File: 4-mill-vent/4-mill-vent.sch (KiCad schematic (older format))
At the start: 73 parts, among them J1 Fan, J2 Buzzer, J3 Power, J4 ICSP, Q1 MMBT3904, Q2 MMBT3904, Q3 PZT3904, Q4 PZT3904, Q5 TSM480P06CP, Q6 MMBT3904, SW1 Power_off, SW2 Power_On, SW3 Fan_Down, SW4 Fan_Up, U1 LM321, U2 TSR_1-24120, U3 LM1117-5.0, U4 ATmega328P-AU, Y1 16.000MHZ

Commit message: Just pushing updates
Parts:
- added D14: 1N914, Diode_SMD:D_1206_3216Metric, symbol Diode:1N914
- added Q7: MMBT3904, Package_TO_SOT_SMD:SOT-23, symbol Transistor_BJT:MMBT3904
- added R24: 100k, Resistor_SMD:R_0603_1608Metric, symbol Device:R_Small_US
- D3: value SML4752HE3_A/I -> 833-3SMAJ5936B-TP
- R18: value 1k -> 10k
- U2: value TSR_1-24120 -> TPSM84212EAB
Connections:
- net +5V: now also R18.1
- net GND: now also Q7.2 (E)
- net Micro_power_Down: now also D14.2 (A); no longer R18.2
- net Monitor: now also SW2.1, D14.1 (K); no longer R18.1, U4.12 (PB0)
- net Motor: no longer U4.13 (PB1)
- net Up: now also R23.1
- net at R15.2, SW1.2: no longer SW2.1
- net at D13.2 (A), J3.1 (Pin_1): now also R24.2
- new net: Q7.1 (B), R24.1
- new net Ext_Power: Q7.3 (C), R18.2
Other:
- note added: "Batt Voltage Monitor\n30V in 4.5V out divided by 6.66\nfor 20V in the values are 33k and 8.2k for divide by 4\nThe input is clamped at 30v Max, over this the fuse will blow"
- note added: "Micro_Power_Down is active low output from the Micro.\nLatching this line low will power down the unit.\n\nMonitor is active low input to the Micro.\nWhen low this signals the Micro the Power_Off button is depressed\nUp is debounced in hardware.\nDo Not USE Int Pull Up.\n\nExt_Power is active low input to the Micro.\nWhen low this tell the Micro that an Ext Batt is in use.\nDo Not USE Int Pull Up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"
- note added: "Power Block:\n\nPin#1 Ext 30V Batt power \nPin#2 Return Batt Power\nPin#3 Int 30V Batt power"
- note removed: "1951-2612-ND"
- note removed: "Batt Voltage Monitor\n30V in 4.5V out divided by 6.66\nfor 20V in the values are 33k and 8.2k for divide by 4\nThe input is clamped at 33v Max, over this the fuse will blow"
- note removed: "Power Block:\n\nPin#1 INT 30V Batt power \nPin#2 Return Batt Power (Black)\nPin#3 EXT 30V Batt power"
- moved on the sheet: C10, C11, C12, C13, C14, C15, C16, C4, C7, C8, C9, D11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

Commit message: Just an update on things
update schematic to and pcb. figured out a way to user int, ext and chager over three pin connector with only to wires to PCB and no extra diode needed. getting closer to the anwers on PWM pins to use with what fuction.
very little let to do on PCB, but things have to get checked before getting it done.
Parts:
- removed D13: FM4004-W, Diode_SMD:D_SMB, symbol Diode:1N4003
- removed J3: Power, Connector_Molex:Molex_KK-254_AE-6410-03A_1x03_P2.54mm_Vertical, symbol Connector:Conn_01x03_Male
- removed Q7: MMBT3904, Package_TO_SOT_SMD:SOT-23, symbol Transistor_BJT:MMBT3904
- removed R18: 10k, Resistor_SMD:R_0603_1608Metric, symbol Device:R_Small_US
- removed R24: 100k, Resistor_SMD:R_0603_1608Metric, symbol Device:R_Small_US
- added BT1, BT2: Battery, symbol Device:Battery
- added J3: POWER_CONNECTOR, Connector_Molex:Molex_KK-254_AE-6410-02A_1x02_P2.54mm_Vertical, symbol Connector:Conn_01x02_Male
- added J5: Charger connector, symbol Connector:Conn_01x03_Female
- added J6: Ext connector, symbol Connector:Conn_01x03_Male
- added J7: Safety connector, symbol Connector:Conn_01x03_Female
- added J8: Power connector, symbol Connector:Conn_01x02_Female
- added J9: Ext batt connector, symbol Connector:Conn_01x03_Female
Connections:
- net GND: now also J3.1 (Pin_1)
- net Monitor: no longer C10.1, J4.3 (Pin_3), Q6.1 (B), R15.1, R16.1, SW2.1, U4.17 (PB5)
- net Up: no longer J4.4 (Pin_4), U4.15 (PB3)
- net at F1.1: now also J3.2 (Pin_2)
- net Timer_OC2B: now reaches U4.1 (PD3)
- net Timer_OC0A: now reaches U4.10 (PD6)
- net Timer_OC1A: now reaches U4.13 (PB1)
- net Timer_OC1B: now reaches U4.14 (PB2)
- net Timer_OC0B: now reaches U4.9 (PD5)
- net Down renamed Down+MOSO
- net Down+MOSO: now also J4.4 (Pin_4); no longer J4.1 (Pin_1)
- new net: J7.2 (Pin_2), J7.3 (Pin_3)
- new net: BT1.2 (-), J9.1 (Pin_1)
- new net: BT1.1 (+), J9.2 (Pin_2)
- new net: BT2.2 (-), J6.1 (Pin_1), J8.1 (Pin_1)
- new net: BT2.1 (+), J6.2 (Pin_2)
- new net: J6.3 (Pin_3), J8.2 (Pin_2)
- new net Monitor_SCLK: C10.1, J4.3 (Pin_3), Q6.1 (B), R15.1, R16.1, SW2.1, U4.17 (PB5)
- new net Timer_OC2A_MOSI: J4.1 (Pin_1), U4.15 (PB3)
- no-connect marks 1 -> 4
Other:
- note added: "Power Block:\n\nPin#1 Return Batt Power\nPin#2 Int 30V Batt power"
- note removed: "Power Block:\n\nPin#1 Ext 30V Batt power \nPin#2 Return Batt Power\nPin#3 Int 30V Batt power"
- moved on the sheet: D14, D3, F1, J1, J2, R4

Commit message: just keeping files up to date
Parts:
- removed D12: FM4004-W, Diode_SMD:D_SMB, symbol Diode:1N4003
- removed J2: Buzzer, Connector_Molex:Molex_KK-254_AE-6410-02A_1x02_P2.54mm_Vertical, symbol Connector:Conn_01x02_Male
- added D12: 1N914, Diode_SMD:D_1206_3216Metric, symbol Diode:1N914
- added D13: FM4004-W, Diode_SMD:D_SMB, symbol Diode:1N4003
- added J2: Buzzer, symbol Connector:Conn_01x03_Male
- C10: value 1uF -> T491C107M006AT; footprint Capacitor_SMD:C_1206_3216Metric -> Capacitor_Tantalum_SMD:CP_EIA-6032-15_Kemet-U
- C7: value LMK316AB7106MLHT -> 3.3uF
- C8: value C0603C104M4RACTU -> LMK316AB7106MLHT; footprint Capacitor_SMD:C_0603_1608Metric -> Capacitor_SMD:C_1206_3216Metric
- C9: value T491C107M006AT -> C0603C104M4RACTU; footprint Capacitor_Tantalum_SMD:CP_EIA-6032-15_Kemet-U -> Capacitor_SMD:C_0603_1608Metric
- J3: value POWER_CONNECTOR -> Power
- R12: value 100k -> 560k
- R15: value 1M -> 820k
- R16: value 10k -> 220k
- R17: value 47 -> 560k
- SW1: value Power_off -> Power_On
- SW2: value Power_On -> Power_off
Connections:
- net +12V: now also C9.1; no longer C7.1, R16.2
- net +5V: now also D13.1 (K)
- net Buzzer-: now also J2.1 (Pin_1)
- net GND: now also D14.2 (A), R17.2, SW2.1; no longer Q6.2 (E), R17.1, SW1.1
- net Micro_power_Down: now also D12.2 (A); no longer D14.2 (A)
- net Monitor: now also C7.1, Q6.1 (B), R15.1, R16.1, SW1.1; no longer D14.1 (K)
- net Monitor_SCLK: no longer C10.1, Q6.1 (B), R15.1, R16.1, SW2.1
- net Raw_Batt: now also R12.1, R13.2; no longer R12.2, R13.1
- net SW_Batt: now also J2.3 (Pin_3)
- net at Q5.1 (G), Q6.3 (C): now also R12.2; no longer R13.2
- net at SW2.2: now also R16.2, D12.1 (K); no longer R12.1
- net at SW1.2: now also R13.1; no longer R15.2
- net at U3.1 (GND): now also D14.1 (K); no longer R17.2
- net at D11.2 (A), U3.2 (VO): now also C10.1, R15.2, D13.2 (A); no longer C9.1
- net at J6.2 (Pin_2): now also J8.2 (Pin_2); no longer BT2.1 (+)
- net at J6.3 (Pin_3): now also BT2.1 (+); no longer J8.2 (Pin_2)
- net Error renamed LED4
- new net: Q6.2 (E), R17.1
- no-connect marks 4 -> 5
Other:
- note added: "6 Cell LiPo"
- note added: "Buzzer:\nPin#3 Buzzer -\nPin#2 N/C\nPin#1 Buzzer +"
- note added: "tested over 2 second delay off from full load to no load\n5v reg. set to 5.6v for diode drop."
- note removed: "Buzzer:\nPin#2 Buzzer -\nPin#1 Buzzer +"
- moved on the sheet: BT1, BT2, C1, C11, C12, C13, C14, C15, C16, C2, C3, C5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

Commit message: Board mainly done
Layout is done, have things to correct and adjustments to make, but for the most part it is done.
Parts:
- removed BT1, BT2: Battery, symbol Device:Battery
- removed J5: Charger connector, symbol Connector:Conn_01x03_Female
- removed J6: Ext connector, symbol Connector:Conn_01x03_Male
- removed J7: Safety connector, symbol Connector:Conn_01x03_Female
- removed J8: Power connector, symbol Connector:Conn_01x02_Female
- removed J9: Ext batt connector, symbol Connector:Conn_01x03_Female
- J2: footprint (none) -> Connector_Molex:Molex_KK-254_AE-6410-03A_1x03_P2.54mm_Vertical
- R5: value RN73H2BTTD4702B10 -> RN73H2BTTD4322F100
- R9: value RN73H2BTTD7061B10 -> RN73H2BTTD8061F50
- renumbered SW2 to SW1, SW1 to SW2
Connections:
- net Timer_OC0B is gone; now on net PWM: U4.9 (PD5)
- net Timer_OC1B is gone; now on net Up: U4.14 (PB2)
- net Timer_OC2B is gone; now on net RPM: U4.1 (PD3)
- net Alarm: now also U4.31 (PD1)
- net LED1: now also U4.23 (PC0)
- net LED2: now also U4.24 (PC1)
- net LED3: now also U4.25 (PC2)
- net LED4: now also U4.26 (PC3)
- net LED5: now also U4.27 (PC4)
- net LED6: now also U4.28 (PC5)
- net LED7: now also U4.30 (PD0)
- net Micro_power_Down: now also U4.11 (PD7)
- net Monitor: now also U4.2 (PD4)
- net Motor: now also U4.32 (PD2)
- net Down+MOSO renamed MOSO
- net MOSO: no longer R22.2
- net Monitor_SCLK renamed SCLK
- net REF: no longer names the net of U4.20 (AREF)
- net Timer_OC0A: no longer names the net of U4.10 (PD6)
- net Timer_OC1A renamed Down
- net Down: now also R22.2
- net Timer_OC2A_MOSI renamed MOSI
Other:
- note added: "Batt Voltage Monitor\nfor 24v the values are 43.2k (R5) and 8.06k (R9) for divide by 5\nfor 20V the values are 33k and 8.2k for divide by 4\nThe input is clamped at 30v Max, over this the fuse will blow"
- note removed: "6 Cell LiPo"
- note removed: "Batt Voltage Monitor\n30V in 4.5V out divided by 6.66\nfor 20V in the values are 33k and 8.2k for divide by 4\nThe input is clamped at 30v Max, over this the fuse will blow"
- moved on the sheet: J4, R21

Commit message: lastest updates to board
Board is done, just need to do more checking
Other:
- moved on the sheet: C11, C12, C13, C14, C15, C16, D10, D4, D5, D6, D7, D8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

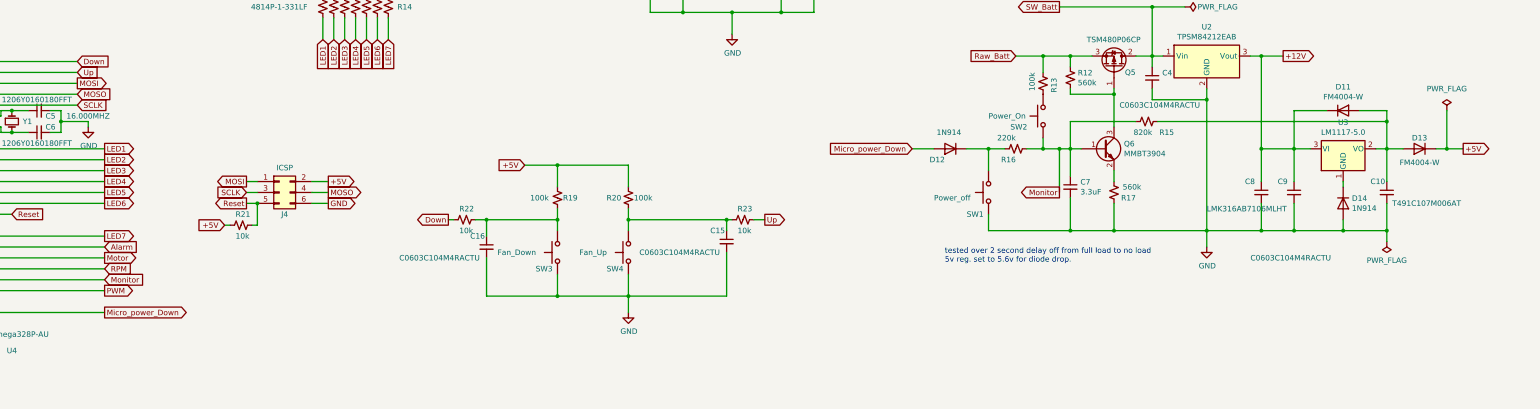
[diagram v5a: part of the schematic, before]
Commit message: Added more to design
Had to add a transitor for allow the micro to power down the unit.
The reason is Q6's base can be as high as 16v when the on button is pressed.
This micro does not have open collector outputs and that would blow the chip.
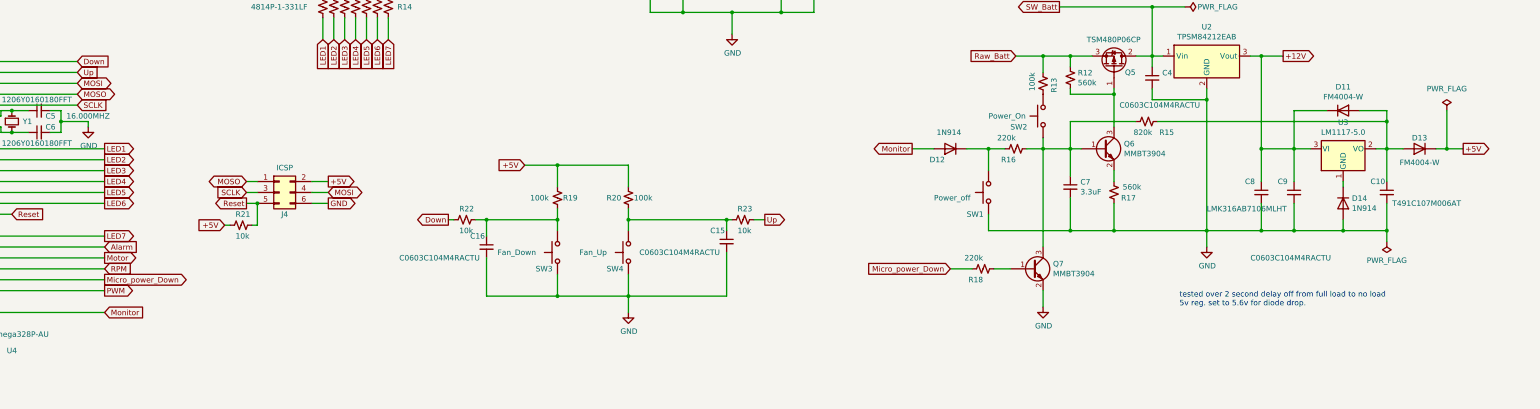
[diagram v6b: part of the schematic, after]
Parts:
- added Q7: MMBT3904, Package_TO_SOT_SMD:SOT-23, symbol Transistor_BJT:MMBT3904
- added R18: 220k, Resistor_SMD:R_0603_1608Metric, symbol Device:R_Small_US
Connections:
- net GND: now also Q7.2 (E)
- net MOSI: now also J4.4 (Pin_4); no longer J4.1 (Pin_1)
- net MOSO: now also J4.1 (Pin_1); no longer J4.4 (Pin_4)
- net Micro_power_Down: now also U4.2 (PD4), R18.2; no longer D12.2 (A), U4.11 (PD7)
- net Monitor: now also D12.2 (A), U4.11 (PD7); no longer C7.1, Q6.1 (B), R15.1, R16.1, SW2.1, U4.2 (PD4)
- new net: Q7.1 (B), R18.1
- new net: C7.1, Q6.1 (B), Q7.3 (C), R15.1, R16.1, SW2.1
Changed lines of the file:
@@
 Wire Wire Line
 	1150 3700 1150 3850
-Text GLabel 3300 4500 2    50   Input ~ 0
+Text GLabel 3300 4500 2    50   BiDi ~ 0
 MOSO
-Text GLabel 3300 4400 2    50   Output ~ 0
+Text GLabel 3300 4400 2    50   BiDi ~ 0
 MOSI
 $Comp
@@
 	9850 650  9850 900
 Connection ~ 10150 650
-Text GLabel 10950 5000 0    50   Input ~ 0
+Text GLabel 11300 6100 0    50   Input ~ 0
 Micro_power_Down
-Text GLabel 3550 6500 2    50   Output ~ 0
+Text GLabel 3550 6200 2    50   Output ~ 0
 Micro_power_Down
 Wire Wire Line
@@
 Text GLabel 3300 4600 2    50   Input ~ 0
 SCLK
-Text GLabel 12300 5400 0    50   Output ~ 0
+Text GLabel 10950 5000 0    50   Output ~ 0
 Monitor
 Text GLabel 6700 5650 0    50   Output ~ 0
@@
 Text GLabel 9600 5650 2    50   Output ~ 0
 Up
-Text GLabel 5600 5400 2    50   Output ~ 0
+Text GLabel 4850 5300 0    50   BiDi ~ 0
 MOSO
-Text GLabel 4850 5300 0    50   Output ~ 0
+Text GLabel 5600 5400 2    50   BiDi ~ 0
 MOSI
 Text GLabel 4850 5400 0    50   Input ~ 0
@@
 	0    -1   -1   0
 $EndComp
-Text Notes 11250 6050 0    50   ~ 0
+Text Notes 13400 6450 0    50   ~ 0
 tested over 2 second delay off from full load to no load\n5v reg. set to 5.6v for diode drop.
 Wire Wire Line
@@
 Connection ~ 12800 5750
 Wire Wire Line
-	12400 5000 12300 5000
-Wire Wire Line
 	12400 4150 12600 4150
 Wire Wire Line
@@
 Wire Wire Line
 	10950 5000 11150 5000
-Wire Wire Line
-	12300 5000 12300 5400
-Text GLabel 3550 6200 2    50   Input ~ 0
+Text GLabel 3550 6500 2    50   Input ~ 0
 Monitor
-Connection ~ 12300 5000
-Wire Wire Line
-	12300 5000 12150 5000
 Wire Wire Line
 	2500 5000 3550 5000
@@
 Wire Wire Line
 	13150 4450 13150 4550
+Wire Wire Line
+	12150 5000 12400 5000
+Wire Wire Line
+	11300 6100 11500 6100
+Wire Wire Line
+	12150 5000 12150 5900
+$Comp
+L Transistor_BJT:MMBT3904 Q7
+U 1 1 5F1B5AF9
+P 12050 6100
+F 0 "Q7" H 12241 6146 50  0000 L CNN
+F 1 "MMBT3904" H 12241 6055 50  0000 L CNN
+F 2 "Package_TO_SOT_SMD:SOT-23" H 12250 6025 50  0001 L CIN
+F 3 "https://www.fairchildsemi.com/datasheets/2N/2N3904.pdf" H 12050 6100 50  0001 L CNN
+	1    12050 6100
+	1    0    0    -1
+$EndComp
+$Comp
+L Device:R_Small_US R18
+U 1 1 5F1F10F9
+P 11600 6100
+F 0 "R18" V 11700 6100 50  0000 R CNN
+F 1 "220k" V 11500 6100 50  0000 R CNN
+F 2 "Resistor_SMD:R_0603_1608Metric" H 11600 6100 50  0001 C CNN
+F 3 "~" H 11600 6100 50  0001 C CNN
+	1    11600 6100
+	0    1    1    0
+$EndComp
+Wire Wire Line
+	11850 6100 11700 6100
+$Comp
+L power:GND #PWR0101
+U 1 1 5F23F3F8
+P 12150 6450
+F 0 "#PWR0101" H 12150 6200 50  0001 C CNN
+F 1 "GND" H 12155 6277 50  0000 C CNN
+F 2 "" H 12150 6450 50  0001 C CNN
+F 3 "" H 12150 6450 50  0001 C CNN
+	1    12150 6450
+	1    0    0    -1
+$EndComp
+Wire Wire Line
+	12150 6300 12150 6450
 $EndSCHEMATC

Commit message: Made debounce failsafe
found a missing resistor on raw rpm pull up. other little error or problems were fixed as well. all part of normal clean up
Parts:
- added D11, D12: 1N914, Diode_SMD:D_1206_3216Metric, symbol Diode:1N914
- added R4: 10k, Resistor_SMD:R_0603_1608Metric, symbol Device:R_Small_US
- R24: renamed from R18; value 220k -> 4.7k
- R9: renamed from R7; value 10k -> 4.7k
- renumbered C4 to C10, C15 to C11, C16 to C12, C7 to C13, C8 to C14, C9 to C15, C10 to C16, C11 to C2, C12 to C3, C13 to C4, C14 to C5, C2 to C6, C3 to C7, C5 to C8, C6 to C9, D11 to D13, D12 to D14, D13 to D15, D14 to D16, R8 to R10, R10 to R11, R11 to R12, R14 to R13, R19 to R14, R20 to R15, R12 to R16, R13 to R17, R22 to R18, R23 to R19, R21 to R20, R15 to R21, R16 to R22, R17 to R23, R4 to R6, R6 to R7, R9 to R8, U4 to U2, U2 to U3, U3 to U4
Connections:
- net +5V: now also R4.2
- net Down: now also C12.1, D11.1 (K)
- net Raw_RPM: now also R4.1
- net Up: now also C11.1, D12.1 (K)
- net at R14.1, R18.1, SW3.2: now also D11.2 (A); no longer C12.1
- net at R15.1, R19.2, SW4.2: now also D12.2 (A); no longer C11.1
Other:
- note added: "Micro_Power_Down is active High output from the Micro.\nLatching this line low will power down the unit.\n\nExt_Power is active low input to the Micro.\nWhen low this tell the Micro that an Ext Batt is in use.\nDo Not USE Int Pull Up.\n\nUp is active low input to the Micro.\nWhen low this signals the Micro the Up button is depressed.\nUp is debounced in hardware.\nDo Not USE Int Pull Up.\n\nDown 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"
- note removed: "Micro_Power_Down is active low output from the Micro.\nLatching this line low will power down the unit.\n\nMonitor is active low input to the Micro.\nWhen low this signals the Micro the Power_Off button is depressed\nUp is debounced in hardware.\nDo Not USE Int Pull Up.\n\nExt_Power is active low input to the Micro.\nWhen low this tell the Micro that an Ext Batt is in use.\nDo Not USE Int Pull Up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"
- moved on the sheet: C10, C11, C12, C13, C14, C15, C16, D13, D14, D15, D16, J4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

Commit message: more clean up
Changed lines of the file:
@@
 Wire Wire Line
 	7900 5650 7900 5750
-Text Notes 9450 2250 0    50   ~ 0
+Text Notes 8750 2350 0    50   ~ 0
 Batt Voltage Monitor\nfor 24v the values are 43.2k (R5) and 8.06k (R9) for divide by 5\nfor 20V the values are 33k and 8.2k for divide by 4\nThe input is clamped at 30v Max, over this the fuse will blow
 $Comp
